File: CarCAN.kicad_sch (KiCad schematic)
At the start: 14 parts, among them IC1 TCAN337DCNR, J2 CANConnector, U13 CDSOT23-T24CAN, U14 MCP2515-E/STVAO, Y4 8 MHz

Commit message: small changes for ravi
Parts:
- removed C42: ~, symbol Device:C
- removed D5: D, symbol Device:D
- removed R25: R, symbol Device:R
- added C36, C68, C69: 100 n, symbol Device:C
- added R34: 10 k, symbol Device:R
- added R35: 10 k, Resistor_SMD:R_0805_2012Metric, symbol Device:R
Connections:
- net +3.3V_PWR: now also C36.1, C68.1, C69.1, R34.1, R35.1
- net Fault: now also R35.2
- net GND: now also C36.2, C68.2, C69.2
- net at U14.19 (~{RESET}): now also R34.2
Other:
- note added: "Need to redo capacitor values once crystal is finalized."
- note added: "Will need to issue RESET command via software."

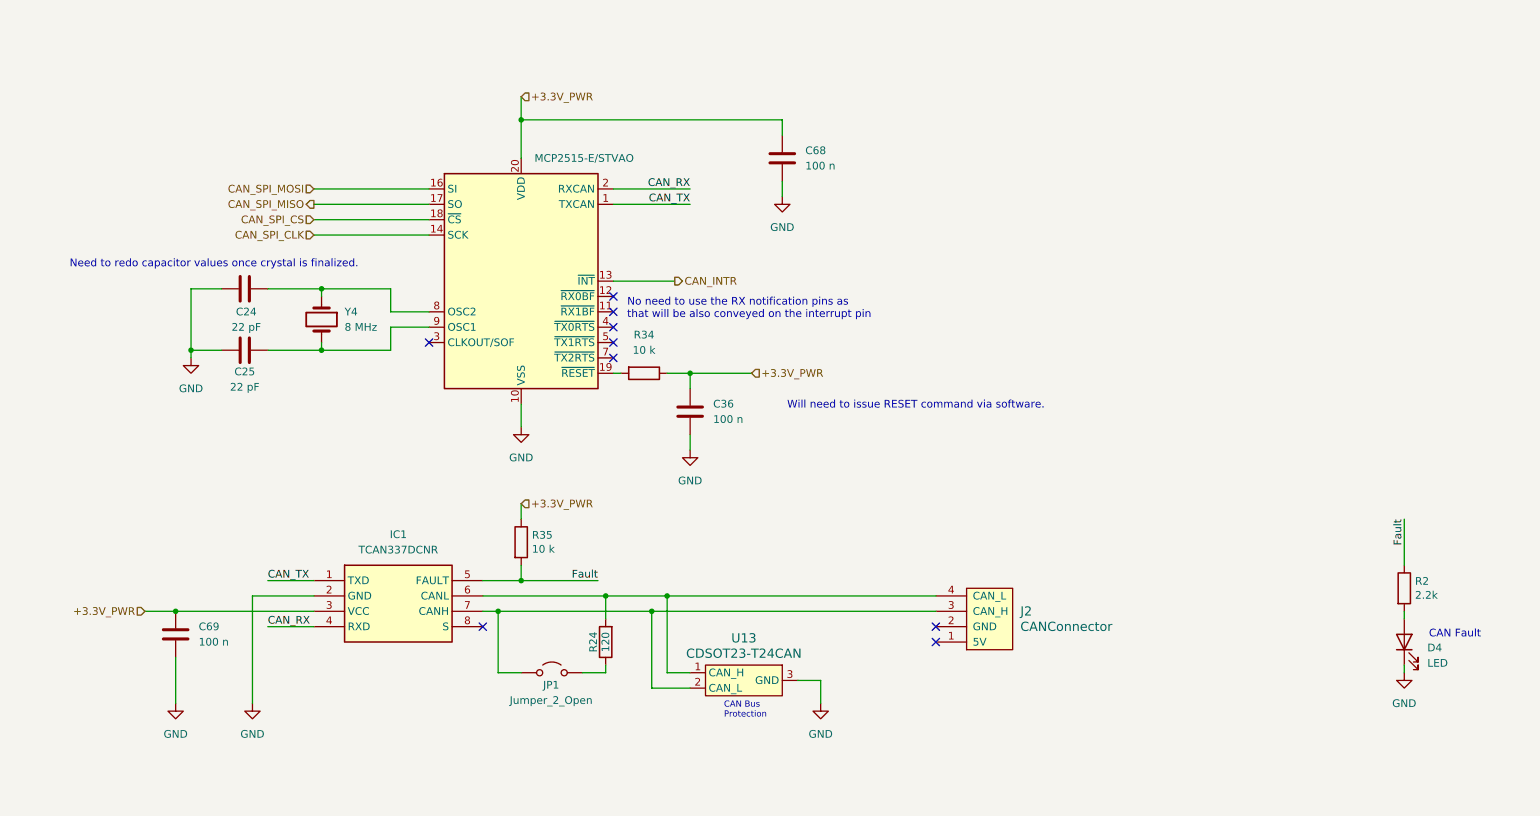
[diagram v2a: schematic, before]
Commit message: added parts to almost everything (except can xtal and fuses)
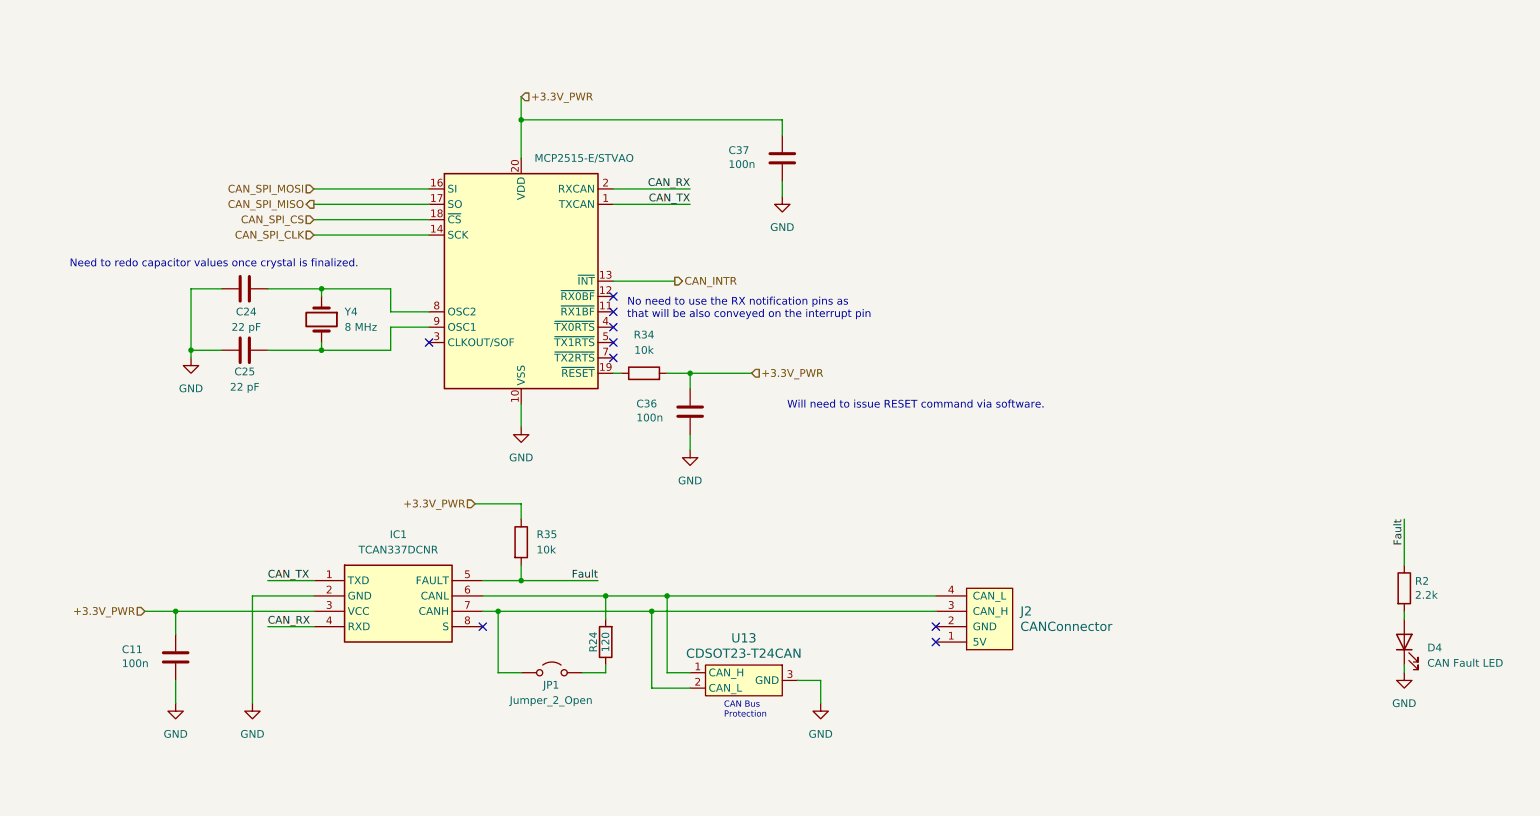
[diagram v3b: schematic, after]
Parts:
- removed C68, C69: 100 n, symbol Device:C
- added C11, C37: 100n, Capacitor_SMD:C_0805_2012Metric, symbol Device:C
- C36: value 100 n -> 100n; footprint (none) -> Capacitor_SMD:C_0805_2012Metric; P/N (none) -> C0805C104M5RACTU
- D4: value LED -> CAN Fault LED; Mouser Part Number 604-APTD2012LCGCK -> (none); P/N APTD2012LCGCK -> APTD2012LSURCK
- IC1: Height 1.45 -> (none); Manufacturer_Name Texas Instruments -> (none); Manufacturer_Part_Number TCAN337DCNR -> (none); Mouser Part Number 595-TCAN337DCNR -> (none); Mouser Price/Stock https://www.mouser.co.uk/ProductDetail/Texas-Instruments/TC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 -> (none); P/N (none) -> TCAN337DCNR
- R2: Mouser Part Number Inventory -> (none)
- R24: Mouser Part Number 71-CRCW080559R0FKEA -> (none); P/N CRCW080559R0FKEA -> CRCW1210120RFKEAHP
- R34: value 10 k -> 10k; footprint (none) -> Resistor_SMD:R_0805_2012Metric; P/N (none) -> CRCW080510K0FKEAC
- R35: value 10 k -> 10k; Mouser Part Number Inventory -> (none); P/N SDR10EZPF2200 -> CRCW080510K0FKEAC
- U13: P/N (none) -> CDSOT23-T24CAN
- U14: Mouser link https://www.mouser.com/ProductDetail/Microchip-Technology/M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 -> (none); P/N (none) -> MCP2515-E/STVAO
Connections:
- net +3.3V_PWR: now also R34.2, C11.1, C37.1; no longer R34.1
- net GND: now also C11.2, C37.2
- net at U14.19 (~{RESET}): now also R34.1; no longer R34.2
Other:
- note removed: "CAN Fault"

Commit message: fixed cap sizes, added remaining parts, fixed rtc battery
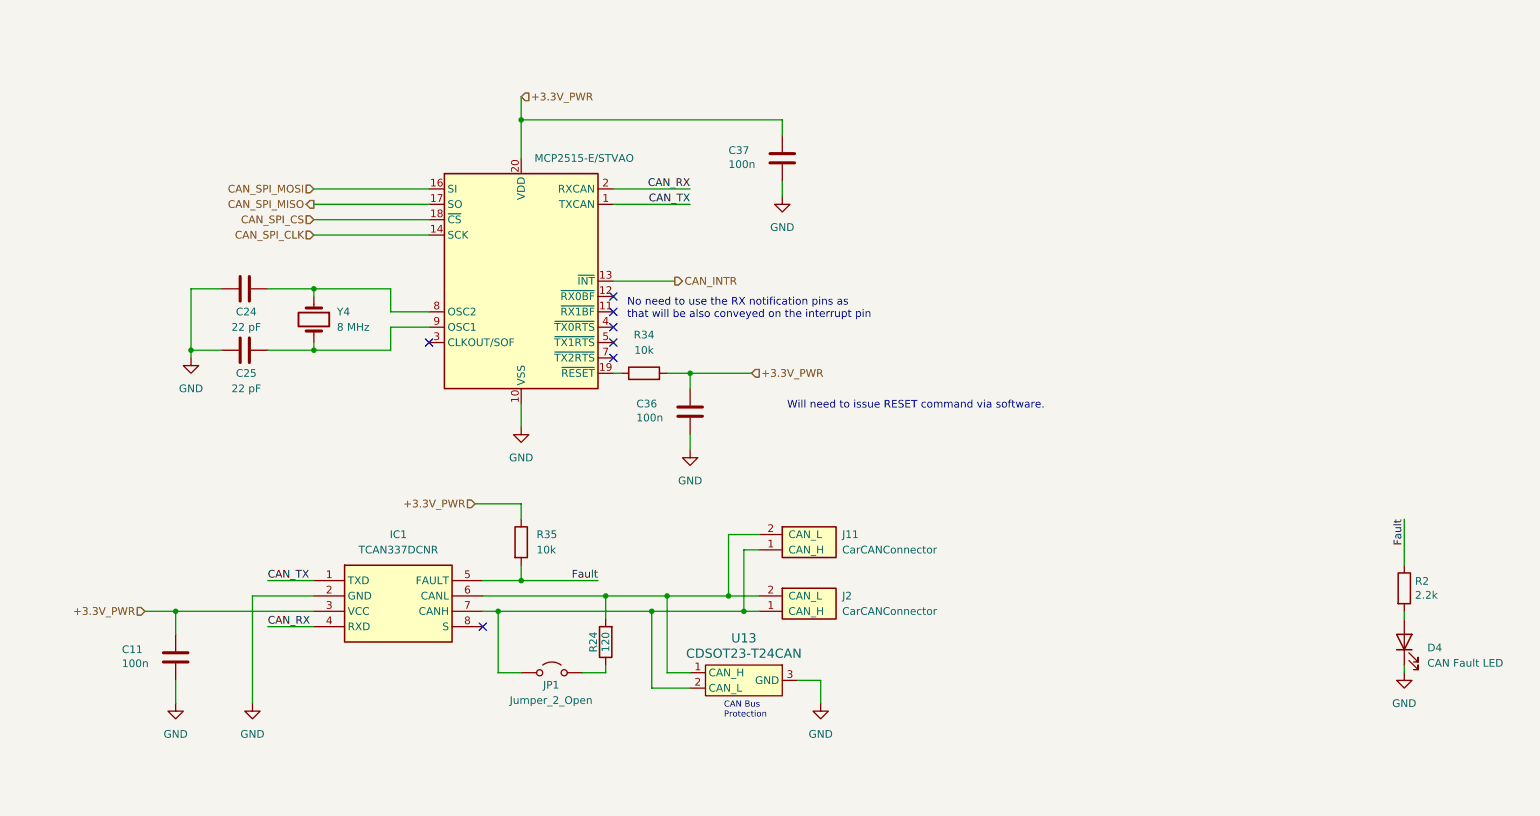
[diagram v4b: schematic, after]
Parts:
- removed IC1: TCAN337DCNR, UTSVT_ICs:SOT65P280X145-8N, symbol utsvt-chips:TCAN337DCNR
- removed J2: CANConnector, UTSVT_Connectors:Molex_MicroFit3.0_1x4xP3.00mm_PolarizingPeg_Vertical, symbol utsvt-connectors:CANConnector
- added IC1: TCAN337DCNR, Controls_Pi:SOT65P280X145-8N, symbol TCAN337DCNR:TCAN337DCNR
- added J11, J2: CarCANConnector, Connector_Molex:Molex_Micro-Fit_3.0_43650-0215_1x02_P3.00mm_Vertical, symbol Connector_Generic:Conn_01x02
- C24, C25: footprint (none) -> Capacitor_SMD:C_0805_2012Metric; P/N (none) -> C0805C220J5HACTU
- Y4: footprint (none) -> Controls_Pi:ABM3; P/N (none) -> ABM3-8.000MHZ-D2Y-T
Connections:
- net +3.3V_PWR: now also IC1.3 (VCC)
- net CAN_RX: now also IC1.4 (RXD)
- net CAN_TX: now also IC1.1 (TXD)
- net Fault: now also IC1.5 (FAULT)
- net GND: now also IC1.2 (GND)
- net at R24.2, U13.1 (CAN_H): now also IC1.6 (CANL), J11.2 (CAN_L), J2.2 (CAN_L)
- net at JP1.1 (A), U13.2 (CAN_L): now also IC1.7 (CANH), J11.1 (CAN_H), J2.1 (CAN_H)
- no-connect marks 9 -> 7
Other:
- note removed: "Need to redo capacitor values once crystal is finalized."
- moved on the sheet: Y4

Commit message: fixed relevant erc errors
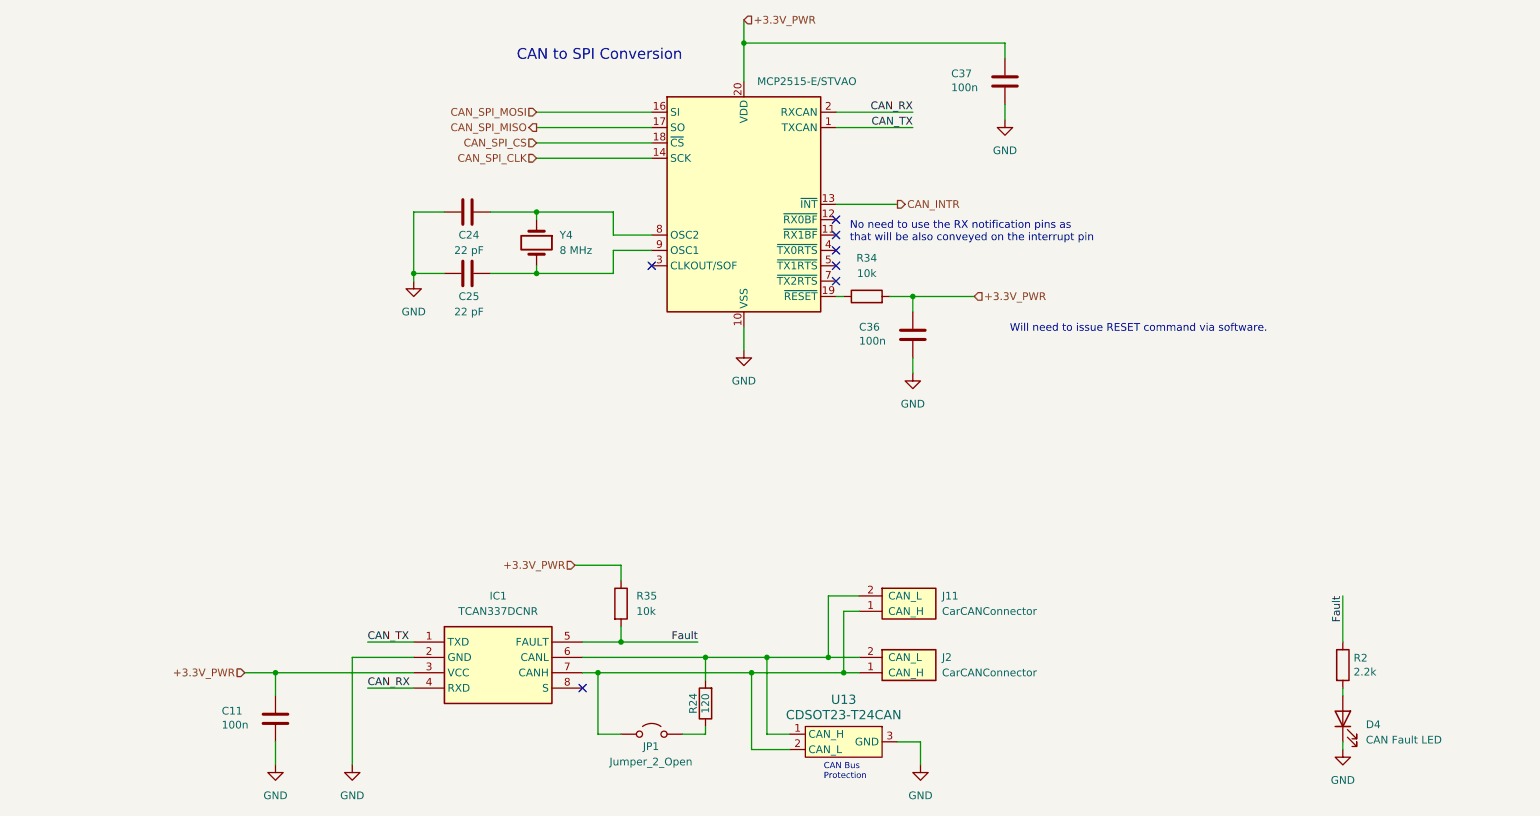
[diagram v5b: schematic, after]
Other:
- note added: "CAN to SPI Conversion"
- moved on the sheet: C11, C24, C25, C36, C37, D4, IC1, J11, J2, JP1, R2, R24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

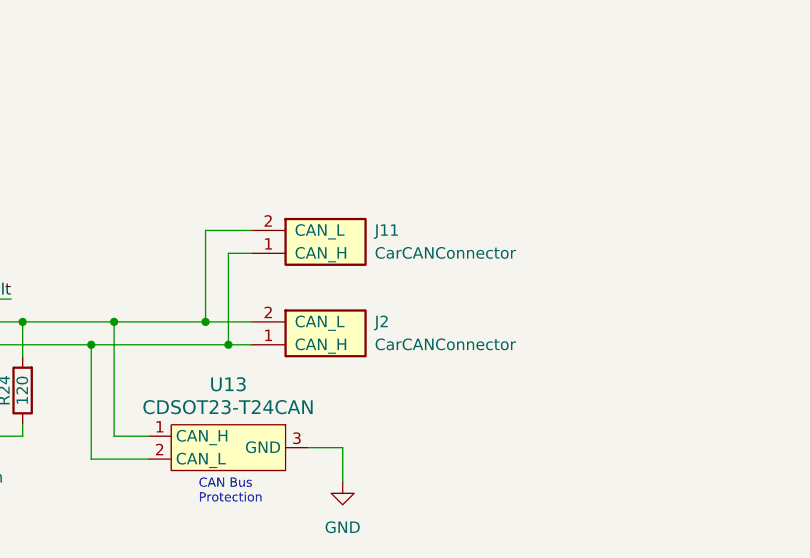
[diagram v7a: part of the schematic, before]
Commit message: fixed erc and removed old schematics
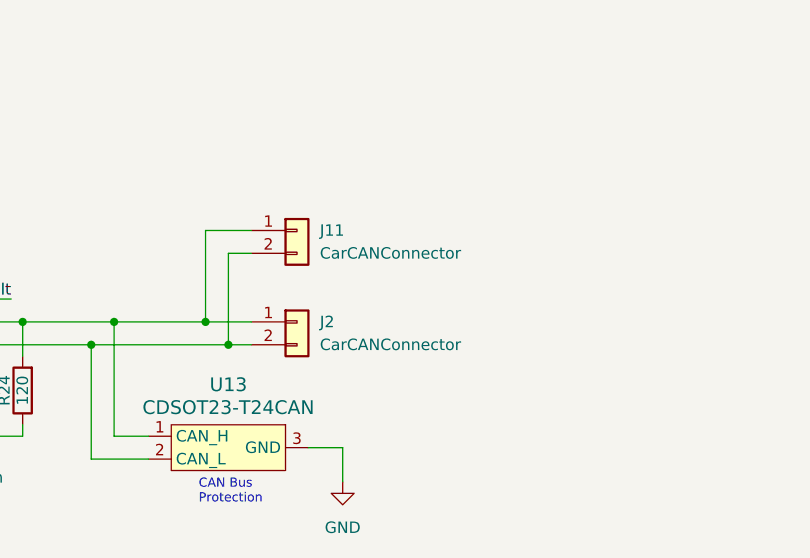
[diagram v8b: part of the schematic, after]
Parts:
- IC1: Arrow Part Number (none) -> TCAN337DCNR; Arrow Price/Stock (none) -> https://www.arrow.com/en/products/tcan337dcnr/texas-instrum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; Height (none) -> 1.45; Manufacturer_Name (none) -> Texas Instruments; Manufacturer_Part_Number (none) -> TCAN337DCNR; Mouser Part Number (none) -> 595-TCAN337DCNR; Mouser Price/Stock (none) -> https://www.mouser.co.uk/ProductDetail/Texas-Instruments/TC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
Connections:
- net at IC1.6 (CANL), R24.2, U13.1 (CAN_H): now also J11.1 (Pin_1), J2.1 (Pin_1); no longer J11.2 (CAN_L), J2.2 (CAN_L)
- net at IC1.7 (CANH), JP1.1 (A), U13.2 (CAN_L): now also J11.2 (Pin_2), J2.2 (Pin_2); no longer J11.1 (CAN_H), J2.1 (CAN_H)
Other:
- moved on the sheet: J11, J2
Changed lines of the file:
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@@
 			)
 		)
-		(property "Datasheet" "https://www.mouser.com/datasheet/2/447/KEM_C1007_X8R_ULTRA_150C_SMD-3316375.pdf"
+		(property "Datasheet" "~"
 			(at 87.63 63.5 0)
 			(effects
@@
 			)
 		)
-		(property "Datasheet" "https://www.mouser.com/datasheet/2/447/KEM_C1002_X7R_SMD-3316098.pdf"
+		(property "Datasheet" "~"
 			(at 161.29 73.66 0)
 			(effects
@@
 			)
 		)
-		(property "Description" "Capacitor 0.1u 20%"
+		(property "Description" "Unpolarized capacitor"
 			(at 161.29 73.66 0)
 			(effects
@@
 			)
 		)
-		(property "Datasheet" "https://www.mouser.com/datasheet/2/216/APTD2012LSURCK-1101937.pdf"
+		(property "Datasheet" "~"
 			(at 232.41 137.16 0)
 			(effects
@@
 			)
 		)
-		(property "Description" "Red LED Vf 1.75, If 2mA"
+		(property "Description" "Light emitting diode"
 			(at 232.41 137.16 0)
 			(effects
@@
 			)
 		)
+		(property "Sim.Pins" "1=K 2=A"
+			(at 232.41 137.16 0)
+			(effects
+				(font
+					(size 1.27 1.27)
+				)
+				(hide yes)
+			)
+		)
 		(pin "1"
 		)
@@
 			)
 		)
-		(property "Datasheet" "https://www.vishay.com/docs/20043/crcwhpe3.pdf"
+		(property "Datasheet" "~"
 			(at 127 134.62 0)
 			(effects
@@
 			)
 		)
-		(property "Description" "Resistor 120 1%"
+		(property "Description" "Resistor"
 			(at 127 134.62 0)
 			(effects
@@
 			)
 		)
-		(property "Datasheet" "https://www.mouser.com/datasheet/2/447/KEM_C1007_X8R_ULTRA_150C_SMD-3316375.pdf"
+		(property "Datasheet" "~"
 			(at 87.63 53.34 0)
 			(effects
@@
 			)
 		)
-		(property "Datasheet" "https://www.vishay.com/docs/28773/crcwce3.pdf"
+		(property "Datasheet" "~"
 			(at 113.03 118.11 0)
 			(effects
@@
 			)
 		)
-		(property "Description" "Resistor 10k 1%"
+		(property "Description" "Resistor"
 			(at 113.03 118.11 0)
 			(effects
@@
 			)
 		)
-		(property "Description" "3.3-V CAN Transceiver"
+		(property "Description" "3.3-V CAN Transceivers"
 			(at 78.74 124.46 0)
 			(effects
@@
 		(property "P/N" "TCAN337DCNR"
 			(at 102.87 719.38 0)
+			(effects
+				(font
+					(size 1.27 1.27)
+				)
+				(justify left top)
+				(hide yes)
+			)
+		)
+		(property "Height" "1.45"
+			(at 102.87 519.38 0)
+			(effects
+				(font
+					(size 1.27 1.27)
+				)
+				(justify left top)
+				(hide yes)
+			)
+		)
+		(property "Manufacturer_Name" "Texas Instruments"
+			(at 102.87 619.38 0)
+			(effects
+				(font
+					(size 1.27 1.27)
+				)
+				(justify left top)
+				(hide yes)
+			)
+		)
+		(property "Manufacturer_Part_Number" "TCAN337DCNR"
+			(at 102.87 719.38 0)
+			(effects
+				(font
+					(size 1.27 1.27)
+				)
+				(justify left top)
+				(hide yes)
+			)
+		)
+		(property "Mouser Part Number" "595-TCAN337DCNR"
+			(at 102.87 819.38 0)
+			(effects
+				(font
+					(size 1.27 1.27)
+				)
+				(justify left top)
+				(hide yes)
+			)
+		)
+		(property "Mouser Price/Stock" "https://www.mouser.co.uk/ProductDetail/Texas-Instruments/TCAN337DCNR?qs=gMfM3zrbS4r1ZrvbjcW09A%3D%3D"
+			(at 102.87 919.38 0)
+			(effects
+				(font
+					(size 1.27 1.27)
+				)
+				(justify left top)
+				(hide yes)
+			)
+		)
+		(property "Arrow Part Number" "TCAN337DCNR"
+			(at 102.87 1019.38 0)
+			(effects
+				(font
+					(size 1.27 1.27)
+				)
+				(justify left top)
+				(hide yes)
+			)
+		)
+		(property "Arrow Price/Stock" "https://www.arrow.com/en/products/tcan337dcnr/texas-instruments?region=nac"
+			(at 102.87 1119.38 0)
 			(effects
 				(font
@@
 			)
 		)
-		(property "Datasheet" "https://www.mouser.com/datasheet/2/447/KEM_C1002_X7R_SMD-3316098.pdf"
+		(property "Datasheet" "~"
 			(at 176.53 31.75 0)
 			(effects
@@
 			)
 		)
-		(property "Description" "Capacitor 0.1u 20%"
+		(property "Description" "Unpolarized capacitor"
 			(at 176.53 31.75 0)
 			(effects
@@
 			)
 		)
-		(property "Datasheet" "https://ww1.microchip.com/downloads/aemDocuments/documents/APID/ProductDocuments/DataSheets/MCP2515-Family-Data-Sheet-DS20001801K.pdf"
+		(property "Datasheet" "http://ww1.microchip.com/downloads/en/DeviceDoc/21801e.pdf"
 			(at 135.89 72.39 0)
 			(effects
@@
 		(on_board yes)
 		(dnp no)
-		(fields_autoplaced yes)
 		(property "Reference" "J2"
-			(at 166.116 127 0)
+			(at 160.02 127 0)
 			(effects
 				(font
@@
 		)
 		(property "Value" "CarCANConnector"
-			(at 166.116 129.54 0)
+			(at 160.02 129.54 0)
 			(effects
 				(font
@@
 			)
 		)
-		(property "Datasheet" "https://www.molex.com/en-us/products/part-detail-pdf/436500215?display=pdf"
+		(property "Datasheet" "~"
 			(at 159.258 119.888 0)
 			(effects
@@
 			)
 		)
-		(property "Datasheet" "https://abracon.com/Resonators/abm3.pdf"
+		(property "Datasheet" "~"
 			(at 99.06 58.42 0)
 			(effects
@@
 			)
 		)
-		(property "Description" "Crystal 8MHz 18pF 140 Ohms"
+		(property "Description" "Two pin crystal"
 			(at 99.06 58.42 0)
 			(effects
@@
 		(on_board yes)
 		(dnp no)
-		(fields_autoplaced yes)
 		(property "Reference" "J11"
-			(at 166.116 116.84 0)
+			(at 160.02 116.84 0)
 			(effects
 				(font
@@
 		)
 		(property "Value" "CarCANConnector"
-			(at 166.116 119.38 0)
+			(at 160.02 119.38 0)
 			(effects
 				(font
@@
 			)
 		)
-		(property "Datasheet" "https://www.molex.com/en-us/products/part-detail-pdf/436500215?display=pdf"
+		(property "Datasheet" "~"
 			(at 159.258 109.728 0)
 			(effects
@@
 			)
 		)
-		(property "Datasheet" "https://fscdn.rohm.com/en/products/databook/datasheet/passive/resistor/chip_resistor/sdr-e.pdf"
+		(property "Datasheet" "~"
 			(at 232.41 128.27 0)
 			(effects
@@
 			)
 		)
-		(property "Datasheet" "https://www.vishay.com/docs/28773/crcwce3.pdf"
+		(property "Datasheet" "~"
 			(at 153.67 67.31 0)
 			(effects
@@
 			)
 		)
-		(property "Description" "Resistor 10k 1%"
+		(property "Description" "Resistor"
 			(at 153.67 67.31 0)
 			(effects
@@
 			)
 		)
-		(property "Datasheet" "https://www.mouser.com/datasheet/2/447/KEM_C1002_X7R_SMD-3316098.pdf"
+		(property "Datasheet" "~"
 			(at 55.88 137.16 0)
 			(effects
@@
 			)
 		)
-		(property "Description" "Capacitor 0.1u 20%"
+		(property "Description" "Unpolarized capacitor"
 			(at 55.88 137.16 0)
 			(effects
